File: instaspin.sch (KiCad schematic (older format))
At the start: 59 parts, among them J1 CONN_01X02, J2 CONN_01X08, J3 CONN_02X05, P1 CONN_01X03, U1 ACPL-M61L, U2 TMS320F28069M, U3 ADM3053, Y1 CSTCE20M0V13C

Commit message: Footprint assignment complete
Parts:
- R1, R10, R11, R12, R13, R2, R3, R4, R5, R6, R7, R8: footprint (none) -> Resistors_SMD:R_0402
- R9: footprint (none) -> Resistors_SMD:R_0805
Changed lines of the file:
@@
 F 0 "R1" H 880 2320 50  0000 L CNN
 F 1 "4.7k" H 880 2260 50  0000 L CNN
-F 2 "" H 850 2300 50  0001 C CNN
+F 2 "Resistors_SMD:R_0402" H 850 2300 50  0001 C CNN
 F 3 "" H 850 2300 50  0000 C CNN
 	1    850  2300
@@
 F 0 "R11" V 2650 7400 50  0000 L CNN
 F 1 "4.7k" V 2650 7150 50  0000 L CNN
-F 2 "" H 2750 7300 50  0001 C CNN
+F 2 "Resistors_SMD:R_0402" H 2750 7300 50  0001 C CNN
 F 3 "" H 2750 7300 50  0000 C CNN
 	1    2750 7300
@@
 F 0 "R12" V 850 7600 50  0000 L CNN
 F 1 "4.7k" V 850 7350 50  0000 L CNN
-F 2 "" H 950 7500 50  0001 C CNN
+F 2 "Resistors_SMD:R_0402" H 950 7500 50  0001 C CNN
 F 3 "" H 950 7500 50  0000 C CNN
 	1    950  7500
@@
 F 0 "R13" V 2650 7600 50  0000 L CNN
 F 1 "4.7k" V 2650 7350 50  0000 L CNN
-F 2 "" H 2750 7500 50  0001 C CNN
+F 2 "Resistors_SMD:R_0402" H 2750 7500 50  0001 C CNN
 F 3 "" H 2750 7500 50  0000 C CNN
 	1    2750 7500
@@
 F 0 "R5" H 1900 4300 50  0000 L CNN
 F 1 "170 0.5%" H 1700 4200 50  0000 L CNN
-F 2 "" H 2100 4200 50  0001 C CNN
+F 2 "Resistors_SMD:R_0402" H 2100 4200 50  0001 C CNN
 F 3 "" H 2100 4200 50  0000 C CNN
 	1    2100 4200
@@
 F 0 "R6" H 1900 4550 50  0000 L CNN
 F 1 "330 0.5%" H 1700 4450 50  0000 L CNN
-F 2 "" H 2100 4500 50  0001 C CNN
+F 2 "Resistors_SMD:R_0402" H 2100 4500 50  0001 C CNN
 F 3 "" H 2100 4500 50  0000 C CNN
 	1    2100 4500
@@
 F 0 "R2" V 7650 3000 50  0000 L CNN
 F 1 "33k" V 7750 3000 50  0000 L CNN
-F 2 "" H 7850 3050 50  0001 C CNN
+F 2 "Resistors_SMD:R_0402" H 7850 3050 50  0001 C CNN
 F 3 "" H 7850 3050 50  0000 C CNN
 	1    7850 3050
@@
 F 0 "R3" V 7950 3000 50  0000 L CNN
 F 1 "17k" V 8050 3000 50  0000 L CNN
-F 2 "" H 8150 3050 50  0001 C CNN
+F 2 "Resistors_SMD:R_0402" H 8150 3050 50  0001 C CNN
 F 3 "" H 8150 3050 50  0000 C CNN
 	1    8150 3050
@@
 F 0 "R4" V 8300 3100 50  0000 L CNN
 F 1 "330" V 8450 3050 50  0000 L CNN
-F 2 "" H 8400 3250 50  0001 C CNN
+F 2 "Resistors_SMD:R_0402" H 8400 3250 50  0001 C CNN
 F 3 "" H 8400 3250 50  0000 C CNN
 	1    8400 3250
@@
 F 0 "R7" H 850 4750 50  0000 L CNN
 F 1 "1k" H 850 4650 50  0000 L CNN
-F 2 "" H 1050 4650 50  0001 C CNN
+F 2 "Resistors_SMD:R_0402" H 1050 4650 50  0001 C CNN
 F 3 "" H 1050 4650 50  0000 C CNN
 	1    1050 4650
@@
 F 0 "R8" H 850 5050 50  0000 L CNN
 F 1 "1k" H 850 4950 50  0000 L CNN
-F 2 "" H 1050 4950 50  0001 C CNN
+F 2 "Resistors_SMD:R_0402" H 1050 4950 50  0001 C CNN
 F 3 "" H 1050 4950 50  0000 C CNN
 	1    1050 4950
@@
 F 0 "R10" H 9150 5300 50  0000 L CNN
 F 1 "10k" H 9100 5400 50  0000 L CNN
-F 2 "" H 9300 5350 50  0001 C CNN
+F 2 "Resistors_SMD:R_0402" H 9300 5350 50  0001 C CNN
 F 3 "" H 9300 5350 50  0000 C CNN
 	1    9300 5350
@@
 F 0 "R9" H 9500 4900 50  0000 L CNN
 F 1 "120" H 9450 5000 50  0000 L CNN
-F 2 "" H 9400 5050 50  0001 C CNN
+F 2 "Resistors_SMD:R_0805" H 9400 5050 50  0001 C CNN
 F 3 "" H 9400 5050 50  0000 C CNN
 	1    9400 5050

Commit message: Placed SiC module, DC link caps, HV / phase terminals
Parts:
- J2: footprint Connectors_Molex:Connector_Molex_PicoBlade_53261-0871 -> Connectors_Molex:Molex_PicoBlade_53261-0871
- U3: footprint Housings_SOIC:SOIC-20_7.5x12.8mm_Pitch1.27mm -> Housings_SOIC:SOIC-20W_7.5x12.8mm_Pitch1.27mm
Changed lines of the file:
@@
 F 0 "J2" H 9119 2625 50  0000 C CNN
 F 1 "CONN_01X08" H 9119 2716 50  0000 C CNN
-F 2 "Connectors_Molex:Connector_Molex_PicoBlade_53261-0871" H 9200 3200 50  0001 C CNN
+F 2 "Connectors_Molex:Molex_PicoBlade_53261-0871" H 9200 3200 50  0001 C CNN
 F 3 "" H 9200 3200 50  0000 C CNN
 	1    9200 3200
@@
 F 0 "U3" H 8300 5900 50  0000 L CNN
 F 1 "ADM3053" H 9100 5900 50  0000 R CNN
-F 2 "Housings_SOIC:SOIC-20_7.5x12.8mm_Pitch1.27mm" H 8700 4300 50  0001 C CNN
+F 2 "Housings_SOIC:SOIC-20W_7.5x12.8mm_Pitch1.27mm" H 8700 4300 50  0001 C CNN
 F 3 "" H 8400 5850 50  0000 C CNN
 	1    8700 5150

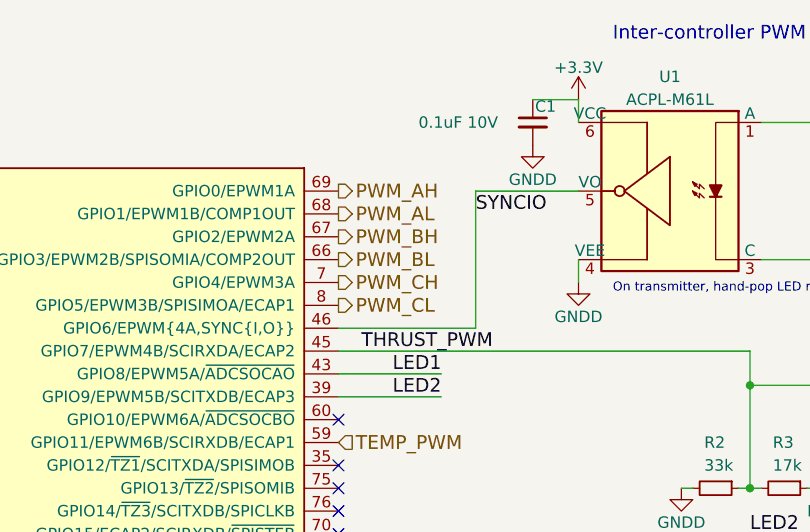
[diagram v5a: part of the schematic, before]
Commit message: Swap PWM nets on 28069M for easier routing
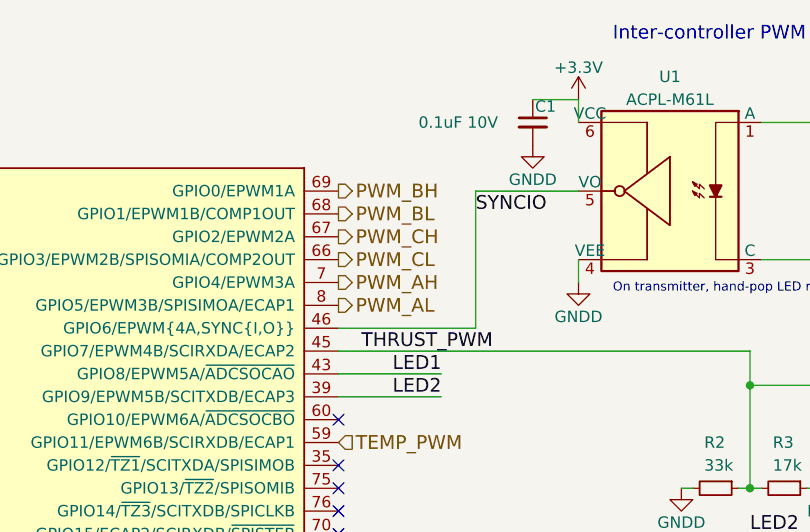
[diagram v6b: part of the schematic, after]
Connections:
- net PWM_AH: now also U2.7 (GPIO4/EPWM3A); no longer U2.69 (GPIO0/EPWM1A)
- net PWM_AL: now also U2.8 (GPIO5/EPWM3B/SPISIMOA/ECAP1); no longer U2.68 (GPIO1/EPWM1B/COMP1OUT)
- net PWM_BH: now also U2.69 (GPIO0/EPWM1A); no longer U2.67 (GPIO2/EPWM2A)
- net PWM_BL: now also U2.68 (GPIO1/EPWM1B/COMP1OUT); no longer U2.66 (GPIO3/EPWM2B/SPISOMIA/COMP2OUT)
- net PWM_CH: now also U2.67 (GPIO2/EPWM2A); no longer U2.7 (GPIO4/EPWM3A)
- net PWM_CL: now also U2.66 (GPIO3/EPWM2B/SPISOMIA/COMP2OUT); no longer U2.8 (GPIO5/EPWM3B/SPISIMOA/ECAP1)
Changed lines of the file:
@@
 TEMP_EN
 Text HLabel 6200 1750 2    60   Output ~ 0
+PWM_BH
+Text HLabel 6200 1950 2    60   Output ~ 0
+PWM_CH
+Text HLabel 6200 2150 2    60   Output ~ 0
 PWM_AH
-Text HLabel 6200 1950 2    60   Output ~ 0
-PWM_BH
-Text HLabel 6200 2150 2    60   Output ~ 0
-PWM_CH
 Text HLabel 6200 1850 2    60   Output ~ 0
+PWM_BL
+Text HLabel 6200 2050 2    60   Output ~ 0
+PWM_CL
+Text HLabel 6200 2250 2    60   Output ~ 0
 PWM_AL
-Text HLabel 6200 2050 2    60   Output ~ 0
-PWM_BL
-Text HLabel 6200 2250 2    60   Output ~ 0
-PWM_CL
 Text HLabel 6200 4550 2    60   Input ~ 0
 ~FLT_DESAT

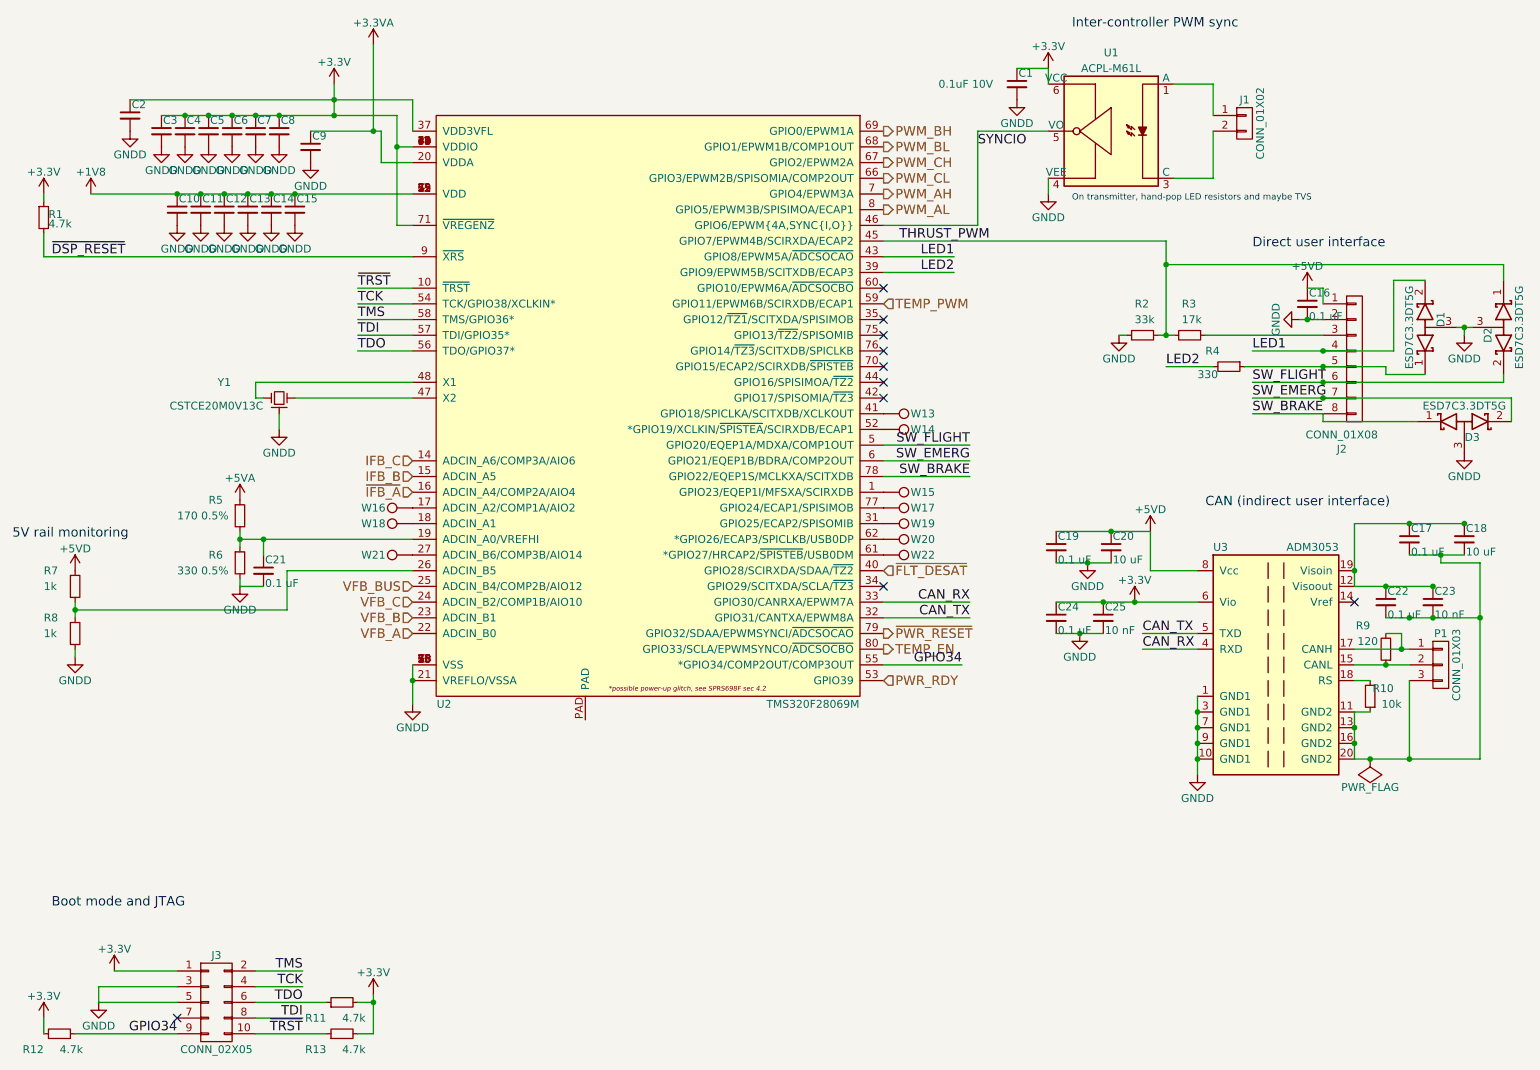
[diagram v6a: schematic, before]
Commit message: Add aux connector for vibe monitor
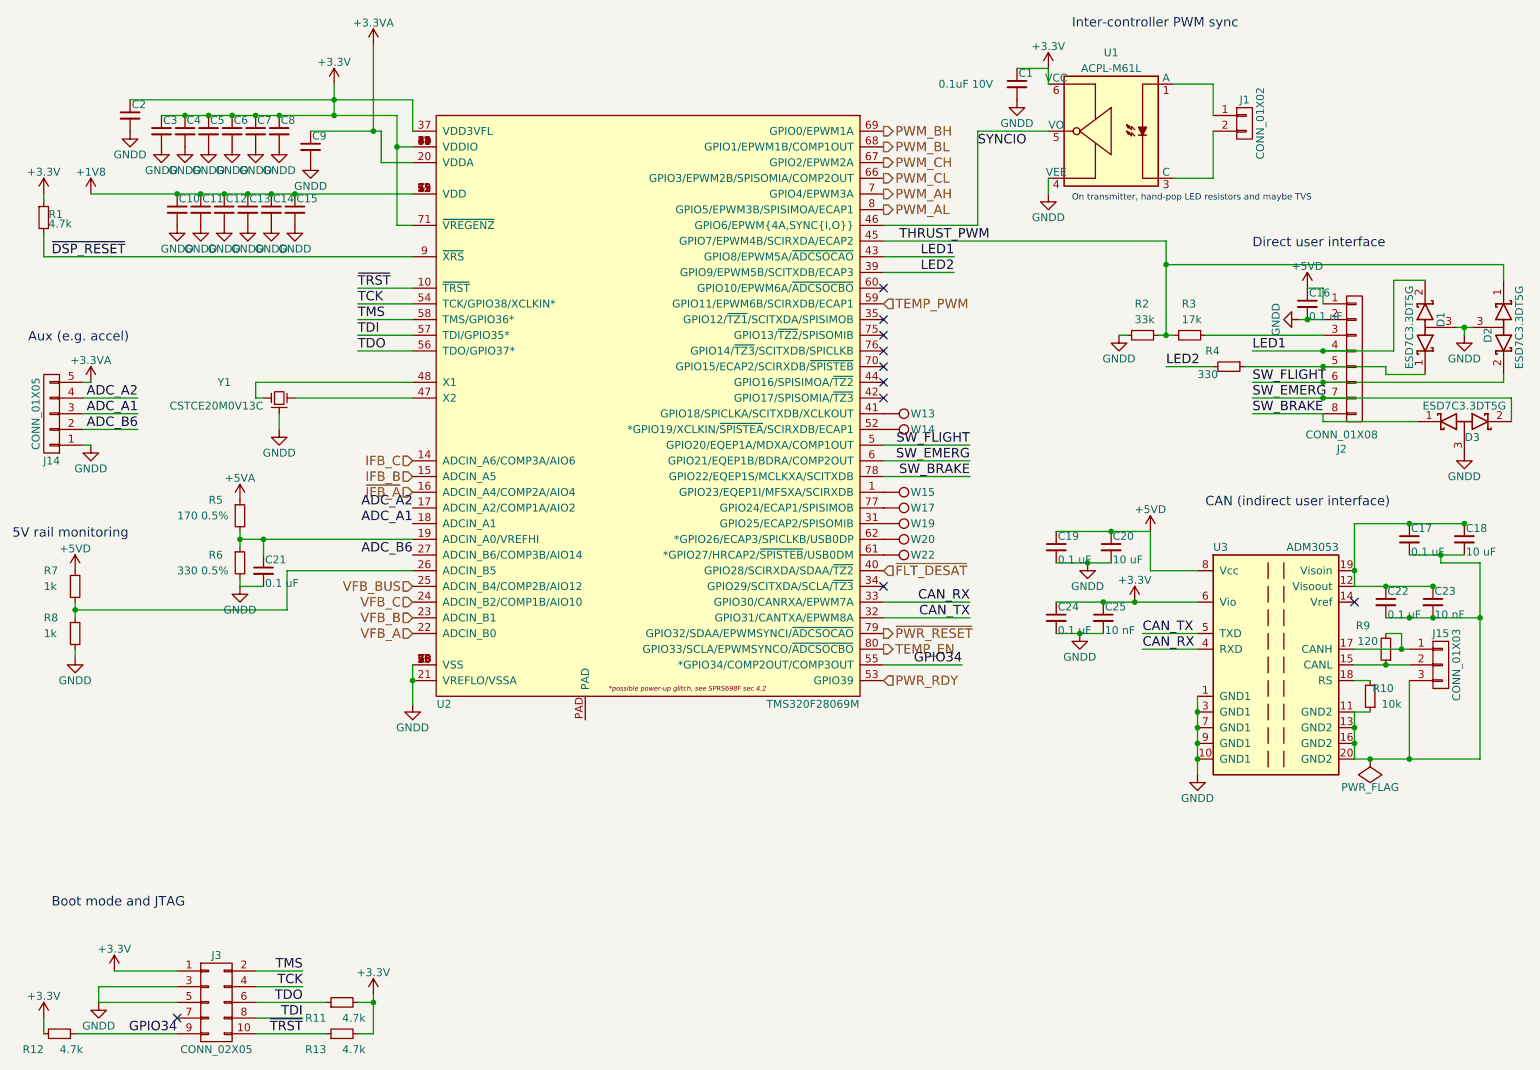
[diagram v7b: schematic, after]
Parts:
- removed W16, W18, W21: TEST_1P, Measurement_Points:Measurement_Point_Round-SMD-Pad_Small, symbol TEST_1P
- added J14: CONN_01X05, Connectors_Molex:Molex_PicoBlade_53261-0571, symbol CONN_01X05
- renumbered P1 to J15
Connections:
- net +3.3VA: now also J14.5 (P5)
- net GNDD: now also J14.1 (P1)
- net ADC_A2: now reaches U2.17 (ADCIN_A2/COMP1A/AIO2)
- net ADC_A2: now also J14.4 (P4)
- net ADC_A1: now reaches U2.18 (ADCIN_A1)
- net ADC_A1: now also J14.3 (P3)
- net ADC_B6: now reaches U2.27 (ADCIN_B6/COMP3B/AIO14)
- net ADC_B6: now also J14.2 (P2)
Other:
- note added: "Aux (e.g. accel)"
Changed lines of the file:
@@
 On transmitter, hand-pop LED resistors and maybe TVS
-$Comp
-L TEST_1P W16
-U 1 1 57F98524
-P 3200 4150
-F 0 "W16" V 3200 4400 50  0000 C CNN
-F 1 "TEST_1P" V 3304 4224 50  0001 C CNN
-F 2 "Measurement_Points:Measurement_Point_Round-SMD-Pad_Small" H 3400 4150 50  0001 C CNN
-F 3 "" H 3400 4150 50  0000 C CNN
-	1    3200 4150
-	0    -1   -1   0
-$EndComp
-$Comp
-L TEST_1P W18
-U 1 1 57F98B51
-P 3200 4250
-F 0 "W18" V 3200 4500 50  0000 C CNN
-F 1 "TEST_1P" V 3304 4324 50  0001 C CNN
-F 2 "Measurement_Points:Measurement_Point_Round-SMD-Pad_Small" H 3400 4250 50  0001 C CNN
-F 3 "" H 3400 4250 50  0000 C CNN
-	1    3200 4250
-	0    -1   -1   0
-$EndComp
-$Comp
-L TEST_1P W21
-U 1 1 57F98BE0
-P 3200 4450
-F 0 "W21" V 3200 4700 50  0000 C CNN
-F 1 "TEST_1P" V 3304 4524 50  0001 C CNN
-F 2 "Measurement_Points:Measurement_Point_Round-SMD-Pad_Small" H 3400 4450 50  0001 C CNN
-F 3 "" H 3400 4450 50  0000 C CNN
-	1    3200 4450
-	0    -1   -1   0
-$EndComp
 $Comp
 L GNDD #PWR033
@@
 $EndComp
 $Comp
-L CONN_01X03 P1
+L CONN_01X03 J15
 U 1 1 57F682F4
 P 9750 5150
-F 0 "P1" H 9750 5350 50  0000 C CNN
+F 0 "J15" H 9750 5350 50  0000 C CNN
 F 1 "CONN_01X03" V 9850 5150 50  0000 C CNN
 F 2 "Connectors_Molex:Molex_PicoBlade_53261-0371" H 9750 5150 50  0001 C CNN
@@
 Text Notes 650  4350 0    60   ~ 0
 5V rail monitoring
+$Comp
+L CONN_01X05 J14
+U 1 1 58061B8A
+P 900 3550
+F 0 "J14" H 900 3850 50  0000 C CNN
+F 1 "CONN_01X05" V 1000 3550 50  0000 C CNN
+F 2 "Connectors_Molex:Molex_PicoBlade_53261-0571" H 900 3550 50  0001 C CNN
+F 3 "" H 900 3550 50  0000 C CNN
+	1    900  3550
+	-1   0    0    1
+$EndComp
+$Comp
+L GNDD #PWR047
+U 1 1 580621EF
+P 1150 3750
+F 0 "#PWR047" H 1150 3500 50  0001 C CNN
+F 1 "GNDD" H 1150 3600 50  0000 C CNN
+F 2 "" H 1150 3750 50  0000 C CNN
+F 3 "" H 1150 3750 50  0000 C CNN
+	1    1150 3750
+	1    0    0    -1
+$EndComp
+Wire Wire Line
+	1150 3750 1100 3750
+$Comp
+L +3.3VA #PWR048
+U 1 1 58062578
+P 1150 3350
+F 0 "#PWR048" H 1150 3200 50  0001 C CNN
+F 1 "+3.3VA" H 1150 3490 50  0000 C CNN
+F 2 "" H 1150 3350 50  0000 C CNN
+F 3 "" H 1150 3350 50  0000 C CNN
+	1    1150 3350
+	1    0    0    -1
+$EndComp
+Wire Wire Line
+	1150 3350 1100 3350
+Wire Wire Line
+	1100 3450 1450 3450
+Wire Wire Line
+	1100 3550 1450 3550
+Wire Wire Line
+	1100 3650 1450 3650
+Text Label 1450 3450 2    60   ~ 0
+ADC_A2
+Text Label 1450 3550 2    60   ~ 0
+ADC_A1
+Text Label 1450 3650 2    60   ~ 0
+ADC_B6
+Text Label 3200 4150 2    60   ~ 0
+ADC_A2
+Text Label 3200 4250 2    60   ~ 0
+ADC_A1
+Text Label 3200 4450 2    60   ~ 0
+ADC_B6
+Text Notes 750  3100 0    60   ~ 0
+Aux (e.g. accel)
 $EndSCHEMATC

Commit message: some logic placement progress
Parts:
- added TIE1: TIE, sictroller:NetTie-_Connected_Small, symbol R
- C10, C11, C12, C13, C14, C15: footprint Capacitors_SMD:C_0603 -> Capacitors_SMD:C_0402
- R7, R8: value 1k -> 10k
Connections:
- net GNDD: now also U2.PAD, TIE1.1; no longer C21.2, C9.2, J14.1 (P1), R6.2, R8.2, U2.21 (VREFLO/VSSA)
- new net GNDA: C21.2, C9.2, J14.1 (P1), R6.2, R8.2, TIE1.2, U2.21 (VREFLO/VSSA)
